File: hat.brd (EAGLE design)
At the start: 65 x 56.5 mm, 23 parts

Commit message: Version 3 ready for public
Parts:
- removed ADS1115: (no value), SparkFun-Connectors:1X10
- removed ADXL345: (no value), SparkFun-Connectors:1X08
- removed D3, D4: (no value), adafruit:DO41-7
- removed D5, D6, D7: TVS, adafruit:DO-1N4148
- added C10: 0.1uF, microbuilder:0805
- added C11, C12: 22pF, microbuilder:0805
- added C4, C5, C9: 0.1µF, microbuilder:0805
- added C6: 10uF, SparkFun-Capacitors:EIA3216
- added C7, C8: 560pF, microbuilder:0805
- added FRAME2: FRAME-LETTERNO_PACKAGE, SparkFun-Aesthetics:DUMMY
- added J3: (no value), SparkFun-Connectors:SCREWTERMINAL-3.5MM-2
- added OK1: 4N35SM, optocoupler:DIL6-SMD
- added R10: 10k, SparkFun-Passives:0805
- added R11: 22k, SparkFun-Passives:0805
- added R12, R7: 4k7, SparkFun-Passives:0805
- added R8, R9: 100, SparkFun-Passives:0805
- added U1: ADS1115IDGST, microbuilder:MSOP10
- added U2: ADXL345, SparkFun-Sensors:LGA14
- added U3: MCP2515-I/SO, mcp2515:SO18L
- added U4: MCP2551, SparkFun-DigitalIC:SO08
- added VD1, VD2: (no value), diode:SOD523
- added X1: 16Mhz, IQD-Frequency-Products:HC49-4-HSMX
- C1, C2: value 100uF -> 10uF; device SparkFun-Passives:CPOL-RADIAL-100UF-25V -> SparkFun-Capacitors:EIA3216
- C3: value 100uF -> 1µF; device SparkFun-Passives:CPOL-RADIAL-100UF-25V -> microbuilder:0805
- D1: device adafruit:DO41-7 -> diode:DO214AC
- D2: device adafruit:DO41-7 -> diode:SOT23
- J1, J2: device SparkFun-Connectors:SCREWTERMINAL-5MM-2 -> SparkFun-Connectors:SCREWTERMINAL-3.5MM-3
- R1, R2, R3, R4, R5: device SparkFun-Passives:AXIAL-0.3 -> SparkFun-Passives:0805
- R6: value 1k -> 10k; device SparkFun-Passives:AXIAL-0.3 -> SparkFun-Passives:0805
- moved C3 56.4 mm to (4.57, 26.4), turned to 270 degrees
- moved C2 51.4 mm to (14.2, 14.2), turned to 90 degrees
- moved GPS 42.4 mm to (61.5, 46.5), turned to 270 degrees
- moved C1 42.0 mm to (31.0, 14.2), turned to 90 degrees
- moved R6 38.7 mm to (12.7, 19.8), turned to 0 degrees
- moved J2 31.5 mm to (16.8, 4.06), turned to 180 degrees
- moved R4 27.5 mm to (17.8, 14.7)
- moved R3 25.9 mm to (20.8, 17.8)
- moved D2 19.7 mm to (22.4, 13.2), turned to 180 degrees
- moved R1 18.1 mm to (23.9, 17.8)
- moved R2 16.1 mm to (26.9, 14.7)
- moved R5 11.4 mm to (42.7, 38.1)
- moved J1 9.40 mm to (27.4, 4.06), turned to 180 degrees
- moved D1 1.70 mm to (37.6, 13.7), turned to 90 degrees
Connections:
- removed net 5.0V: RPI1.2, RPI1.4
- removed net A3: ADS1115.1
- removed net ALRT: ADS1115.5
- removed net BAT-LINKED: ADS1115.2, D7.C
- removed net INT1: ADXL345.4
- removed net INT2: ADXL345.5
- removed net N$1: D1.A, J1.1
- removed net N$10: C3.1, D7.A, R5.P$2, R6.P$2
- removed net N$2: D2.A, J1.2
- removed net N$5: D1.C, R1.P$1
- removed net N$7: D2.C, R3.P$1
- removed net N$9: D3.C, R5.P$1
- new net 5V: C9.1, RPI1.2, RPI1.4, U4.2
- new net BAT-1-INPUT: D2.1, J1.2, R1.1
- new net BAT-2-INPUT: D2.2, J1.3, R3.1
- new net CANH: J3.1, R8.2, U4.7
- new net CANL: J3.2, R9.2, U4.6
- new net LINKED-INPUT: J2.3, R5.1
- new net N$14: C12.1, U3.8, X1.2
- new net N$15: C11.1, U3.7, X1.1
- new net RS: R7.2, U4.8
- new net RXCAN: R10.2, U4.4
- new net SHUNT-HIGH-INPUT: J2.1, U1.6, VD1.C
- new net SHUNT-LOW-INPUT: J2.2, U1.7, VD2.C
- new net TXCAN: U3.1, U4.1
- new net U5_RST: R12.1, U3.17
- new net VEHICLE-GND: D1.C, J1.1
- net 3.3V: now also C10.1, C3.2, C4.1, C5.1, C6.A, R12.2, U1.8, U2.1, U2.12, U2.6, U2.7, U3.18; no longer ADS1115.10, ADXL345.2, ADXL345.3, ADXL345.6
- net ADDR: now also R6.2, U1.1; no longer ADS1115.6
- net BAT-1: now also C1.A, R1.2, R2.2, U1.5; no longer ADS1115.4, D5.C
- net BAT-2: now also C2.A, R3.2, R4.2, U1.4; no longer ADS1115.3, D6.C
- net GND: now also C1.C, C10.2, C11.2, C12.2, C2.C, C3.1, C4.2, C5.2, C6.C, C7.2, C8.2, C9.2, D1.A, D2.3, OK1.2, OK1.4, R11.1, R2.1, R4.1, R6.1, R7.1, U1.3, U2.2, U2.4, U2.5, U3.9, U4.3, VD1.A, VD2.A; no longer ADS1115.9, ADXL345.1, C1.2, C2.2, C3.2, D4.A, R2.P$1, R4.P$1, R6.P$1
- net GPIO25: now also U3.12
- net GPIO5: now also OK1.5
- net N$3: now also OK1.1, R5.2; no longer D3.A, J2.1
- net N$4: now also R10.1, R11.2, U3.2; no longer D4.C, J2.2
- net N$6: now also C7.1, R8.1; no longer C1.1, D5.A, R1.P$2, R2.P$2
- net N$8: now also C8.1, R9.1; no longer C2.1, D6.A, R3.P$2, R4.P$2
- net SCL: now also U1.10, U2.14; no longer ADS1115.8, ADXL345.8
- net SDA: now also U1.9, U2.13; no longer ADS1115.7, ADXL345.7
- net SPI_CE0: now also U3.16
- net SPI_MISO: now also U3.15
- net SPI_MOSI: now also U3.14
- net SPI_SCLK: now also U3.13
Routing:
- net 5V: track 0.00 -> 128.6 mm, vias 0 -> 1
- net LINKED-INPUT: track 0.00 -> 69.4 mm, vias 0 -> 2
- net SDA: track 103.4 -> 49.9 mm, vias 1 -> 2
- net SCL: track 98.0 -> 49.4 mm, vias 1 -> 2
- net N$6: track 43.8 -> 3.63 mm
- net RXD: track 10.5 -> 50.1 mm
- net SHUNT-LOW-INPUT: track 0.00 -> 37.9 mm, vias 0 -> 2
- net TXCAN: track 0.00 -> 37.3 mm
- net TXD: track 16.6 -> 52.8 mm, vias 0 -> 1
- net SHUNT-HIGH-INPUT: track 0.00 -> 35.3 mm, vias 0 -> 2
- net SPI_CE0: track 0.00 -> 35.2 mm, vias 0 -> 1
- net SPI_MISO: track 0.00 -> 31.3 mm, vias 0 -> 2
- net GPIO18: track 18.8 -> 49.8 mm
- net CANL: track 0.00 -> 30.9 mm
- net CANH: track 0.00 -> 29.8 mm
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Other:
- board text added: "Bat 1"
- board text added: "Bat 2"
- board text added: "CAN"
- board text added: "H"
- board text added: "High"
- board text added: "L"
- board text added: "Link"
- board text added: "Low"
- board text added: "RXD-I"
- board text added: "TXD-I"
- board text removed: "GPS-RXD"
- board text removed: "GPS-TXD"
- board text removed: "Jeep Monitoring v1"
- board text removed: "SCL"
- board text removed: "SDA"

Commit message: Cleanup text
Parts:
- FRAME1: value FRAME-LETTER -> FRAME-LETTERNO_PACKAGE; device SparkFun-Aesthetics:CREATIVE_COMMONS -> SparkFun-Aesthetics:DUMMY
- moved FRAME2 74.3 mm to (0.51, 0.51)
- moved FRAME1 9.37 mm to (0.51, 0.25)
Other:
- board text removed: "Andrew LeCody"
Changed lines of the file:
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@@
 <board>
 <plain>
-<text x="34.29" y="-8.89" size="1.778" layer="51">Andrew LeCody</text>
 <text x="59.436" y="36.83" size="1.016" layer="25" rot="R180">GND</text>
 <text x="59.436" y="39.37" size="1.016" layer="25" rot="R180">RXD-I</text>
@@
 <elements>
 <element name="RPI1" library="microbuilder" package="PI_HAT_NOSLOTS" value="RASPBERRYPI_BPLUS_HATNOSLOTS" x="0" y="0"/>
-<element name="FRAME1" library="SparkFun-Aesthetics" package="CREATIVE_COMMONS" value="FRAME-LETTER" x="2.54" y="-8.89"/>
+<element name="FRAME1" library="SparkFun-Aesthetics" package="DUMMY" value="FRAME-LETTERNO_PACKAGE" x="0.508" y="0.254">
+<attribute name="DESIGNER" value="Nobody" x="0.508" y="0.254" size="1.778" layer="27" display="off"/>
+<attribute name="VERSION" value="v01" x="0.508" y="0.254" size="1.778" layer="27" display="off"/>
+</element>
 <element name="GPS" library="SparkFun-Connectors" package="1X05" value="" x="61.468" y="46.482" rot="R270"/>
 <element name="U2" library="SparkFun-Sensors" package="LGA14" value="ADXL345" x="11.684" y="40.64" rot="R90"/>
@@
 <element name="C8" library="microbuilder" package="0805" value="560pF" x="46.736" y="14.732" rot="R180"/>
 <element name="C9" library="microbuilder" package="0805" value="0.1µF" x="45.72" y="20.828" rot="R90"/>
-<element name="FRAME2" library="SparkFun-Aesthetics" package="DUMMY" value="FRAME-LETTERNO_PACKAGE" x="-32.512" y="-66.04">
-<attribute name="DESIGNER" value="Nobody" x="-32.512" y="-66.04" size="1.778" layer="27" display="off"/>
-<attribute name="VERSION" value="v01" x="-32.512" y="-66.04" size="1.778" layer="27" display="off"/>
+<element name="FRAME2" library="SparkFun-Aesthetics" package="DUMMY" value="FRAME-LETTERNO_PACKAGE" x="0.508" y="0.508">
+<attribute name="DESIGNER" value="Nobody" x="0.508" y="0.508" size="1.778" layer="27" display="off"/>
+<attribute name="VERSION" value="v01" x="0.508" y="0.508" size="1.778" layer="27" display="off"/>
 </element>
 <element name="R10" library="SparkFun-Passives" package="0805" value="10k" x="29.972" y="20.32" rot="R270"/>

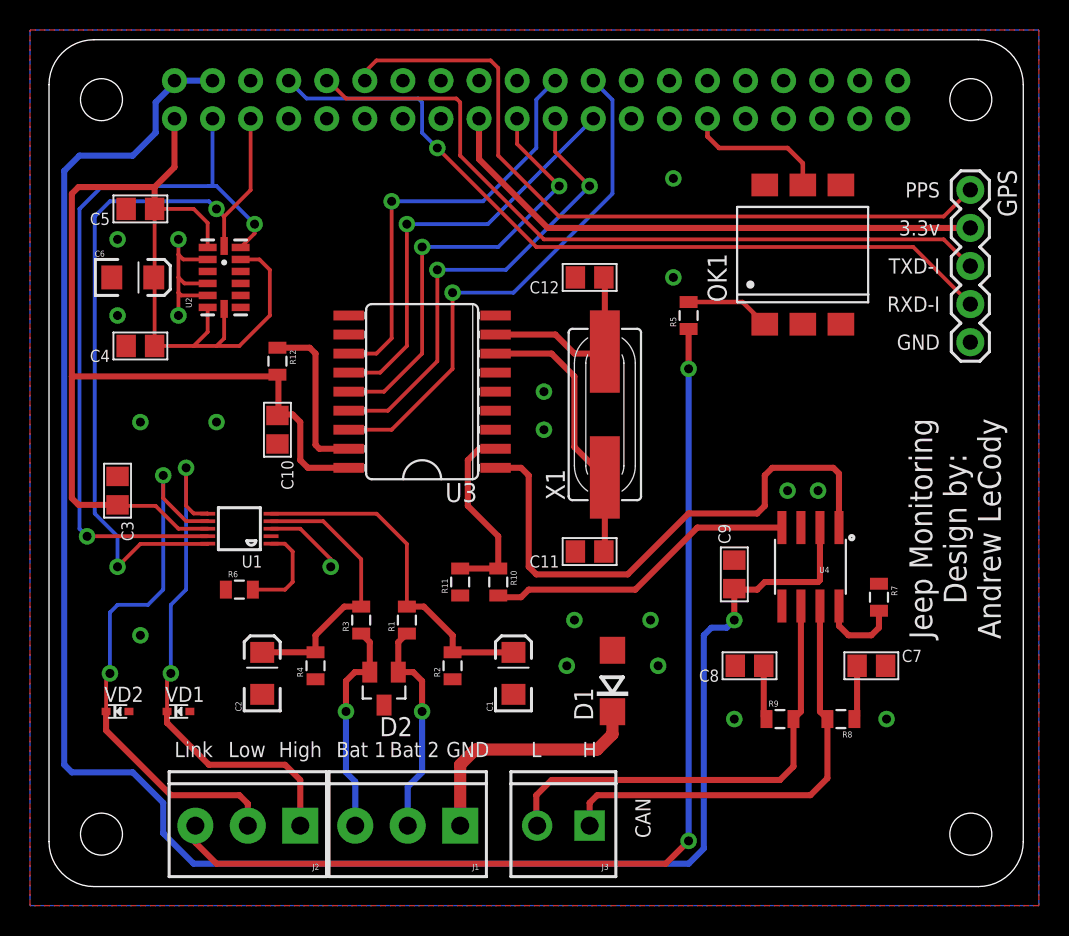
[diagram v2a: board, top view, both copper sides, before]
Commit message: Added 1kOhm resistors on inputs
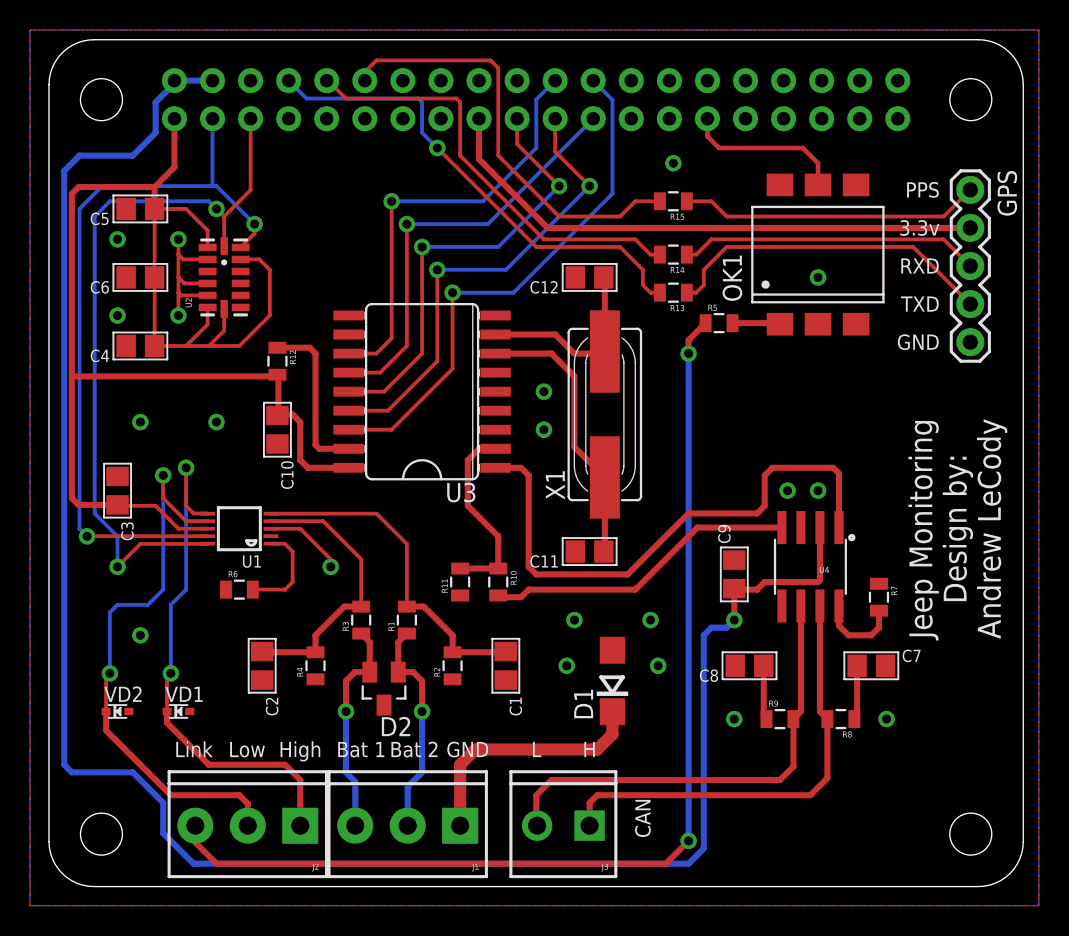
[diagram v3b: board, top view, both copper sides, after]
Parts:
- added R13, R14, R15: 1k, SparkFun-Passives:0805
- C1, C2, C6: value 10uF -> 10µF; device SparkFun-Capacitors:EIA3216 -> microbuilder:0805
- moved R5 2.09 mm to (44.7, 37.6), turned to 0 degrees
- moved OK1 1.02 mm to (51.3, 42.2)
- moved C1 0.72 mm to (30.5, 14.7), turned to 270 degrees
- moved C6 0.51 mm to (6.10, 40.6), turned to 180 degrees
- moved C2 0.51 mm to (14.2, 14.7), turned to 270 degrees
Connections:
- new net N$1: GPS.4, R13.1
- new net N$2: GPS.3, R14.1
- new net N$5: GPS.1, R15.1
- net 3.3V: now also C6.1; no longer C6.A
- net BAT-1: now also C1.1; no longer C1.A
- net BAT-2: now also C2.1; no longer C2.A
- net GND: now also C1.2, C2.2, C6.2; no longer C1.C, C2.C, C6.C
- net GPIO18: now also R15.2; no longer GPS.1
- net RXD: now also R14.2; no longer GPS.3
- net TXD: now also R13.2; no longer GPS.4
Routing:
- net N$1: track 0.00 -> 22.3 mm
- net RXD: track 50.1 -> 29.1 mm
- net GPIO18: track 49.8 -> 28.7 mm
- net TXD: track 52.8 -> 32.4 mm
- net N$2: track 0.00 -> 20.1 mm
- net N$5: track 0.00 -> 20.1 mm
- net N$3: track 5.69 -> 3.19 mm
- net GPIO5: track 9.73 -> 10.8 mm
- net LINKED-INPUT: track 69.4 -> 70.3 mm
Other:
- board text added: "RXD"
- board text added: "TXD"
- board text removed: "RXD-I"
- board text removed: "TXD-I"

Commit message: Changed to packages with larger pads for easier hand soldering
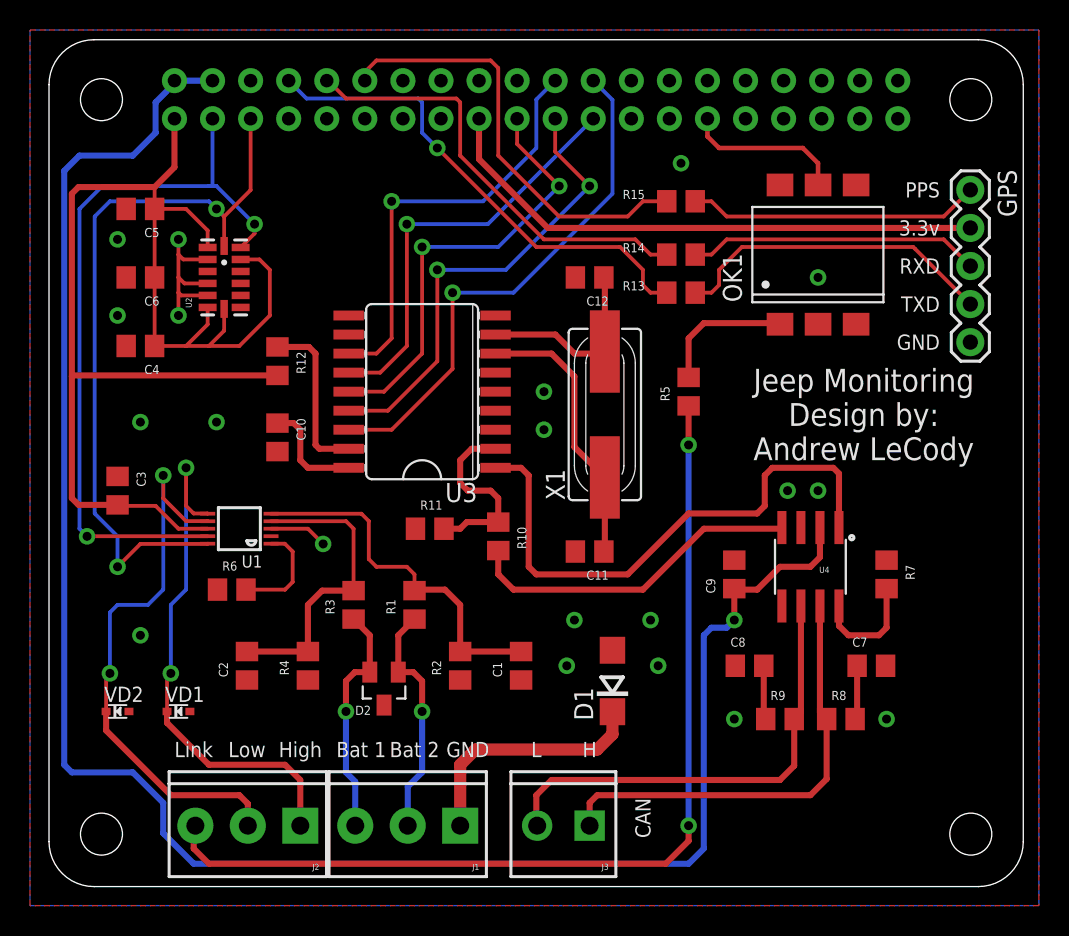
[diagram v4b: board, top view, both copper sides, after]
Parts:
- C1, C2, C6: value 10µF -> 10uF; device microbuilder:0805 -> aceat64-passives:C0805
- C10, C11, C12, C7, C8: device microbuilder:0805 -> aceat64-passives:C0805
- C3: value 1µF -> 1uF; device microbuilder:0805 -> aceat64-passives:C0805
- C4, C5, C9: value 0.1µF -> 0.1uF; device microbuilder:0805 -> aceat64-passives:C0805
- R1, R2, R3, R4: device SparkFun-Passives:0805 -> aceat64-resistor:R0805
- R10, R11, R12, R13, R14, R15, R5, R6, R7, R8, R9: device SparkFun-Passives:0805 -> aceat64-passives:R0805
- moved R5 5.00 mm to (42.7, 33.0), turned to 90 degrees
- moved R11 4.10 mm to (25.4, 23.9), turned to 0 degrees
- moved R10 3.05 mm to (30.0, 23.4)
- moved R7 1.61 mm to (55.9, 20.8)
- moved R1 1.14 mm to (24.4, 18.8)
- moved R3 1.14 mm to (20.3, 18.8)
- moved C2 1.02 mm to (13.2, 14.7)
- moved C1 1.02 mm to (31.5, 14.7)
- moved R13 0.51 mm to (42.2, 39.6)
- moved R14 0.51 mm to (42.2, 42.2)
- moved R15 0.51 mm to (42.2, 45.7)
- moved R4 0.51 mm to (17.3, 14.7)
- moved C10 0.51 mm to (15.2, 30.0)
- moved R2 0.51 mm to (27.4, 14.7)
- moved R6 0.51 mm to (12.2, 19.8)
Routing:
- net N$3: track 3.19 -> 9.15 mm
- net LINKED-INPUT: track 70.3 -> 64.7 mm
- net 3.3V: track 138.4 -> 135.1 mm
- net RS: track 5.59 -> 7.58 mm
- net BAT-1: track 22.7 -> 24.5 mm
- net RXCAN: track 20.9 -> 22.6 mm
- net BAT-2: track 18.8 -> 20.5 mm
- net GND: track 16.6 -> 15.2 mm
- net BAT-2-INPUT: track 14.6 -> 15.7 mm
- net BAT-1-INPUT: track 14.7 -> 15.9 mm
- net 5V: track 128.6 -> 127.7 mm
- net N$2: track 20.1 -> 19.4 mm
- net N$1: track 22.3 -> 21.7 mm
- net N$5: track 20.1 -> 19.5 mm
